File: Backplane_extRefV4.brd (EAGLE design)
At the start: 72.9 x 59.6 mm, 15 parts, among them J1 TFM-125-02-XXX-D-WT

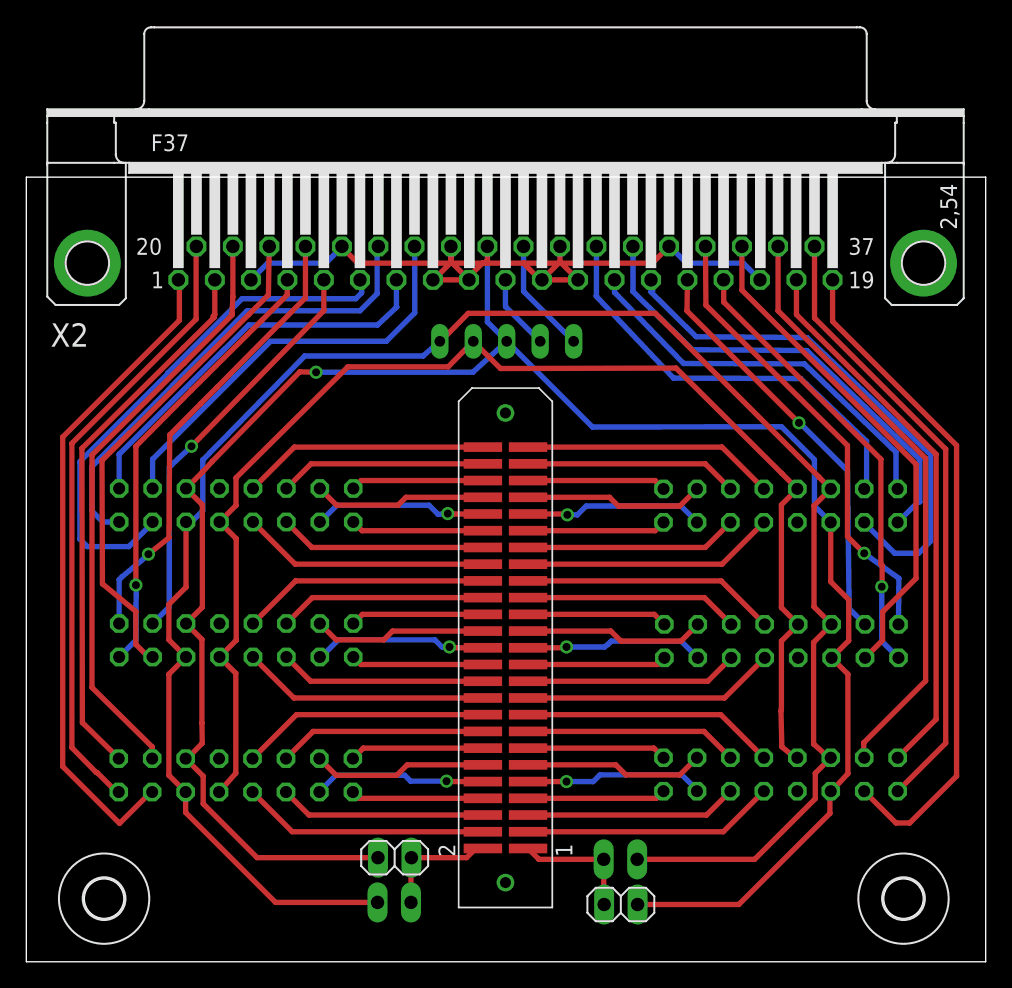
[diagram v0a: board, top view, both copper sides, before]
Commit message: minor labeling and component placement updates. most significant is correcting part position on powerboard so 22uF bypass cap actually connects to ground.
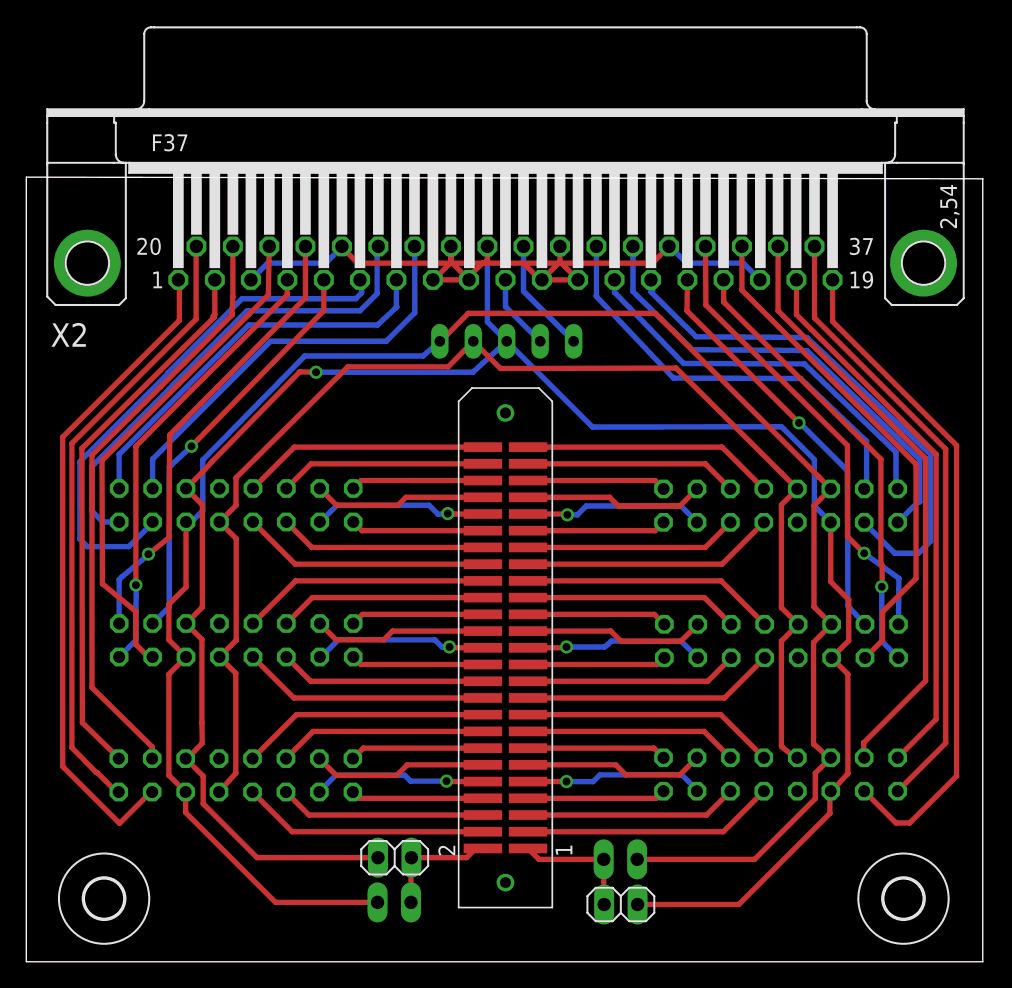
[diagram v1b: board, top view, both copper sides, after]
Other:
- board size 72.9 x 59.6 mm -> 72.6 x 59.6 mm
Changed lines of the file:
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@@
 <board>
 <plain>
-<wire x1="0.0635" y1="0" x2="72.91725" y2="0" width="0" layer="20"/>
-<wire x1="72.91725" y1="0" x2="72.91725" y2="59.58475" width="0" layer="20"/>
-<wire x1="72.91725" y1="59.58475" x2="0.0635" y2="59.58475" width="0" layer="20"/>
+<wire x1="0.0635" y1="0" x2="72.695" y2="0" width="0" layer="20"/>
+<wire x1="72.695" y1="0" x2="72.695" y2="59.45775" width="0" layer="20"/>
+<wire x1="72.695" y1="59.45775" x2="0.0635" y2="59.58475" width="0" layer="20"/>
 <wire x1="0.0635" y1="59.58475" x2="0.0635" y2="0" width="0" layer="20"/>
 <text x="60.706" y="3.39725" size="1.778" layer="26" rot="MR0">G1-&gt;VREF</text>
@@
 </signal>
 <signal name="VCC">
-<wire x1="57.43575" y1="16.3195" x2="57.37225" y2="19.05" width="0.4064" layer="1"/>
-<wire x1="57.37225" y1="19.05" x2="57.404" y2="19.2405" width="0.4064" layer="1"/>
+<wire x1="57.43575" y1="16.3195" x2="57.404" y2="16.383" width="0.4064" layer="1"/>
 <contactref element="SV1" pad="7"/>
 <contactref element="SV2" pad="7"/>
@@
 <wire x1="15.986125" y1="36.750625" x2="15.986125" y2="34.655125" width="0.4064" layer="1"/>
 <wire x1="15.986125" y1="34.655125" x2="14.732" y2="33.401" width="0.4064" layer="1"/>
-<wire x1="57.404" y1="19.2405" x2="57.404" y2="24.35225" width="0.4064" layer="1"/>
+<wire x1="57.404" y1="16.383" x2="57.404" y2="24.35225" width="0.4064" layer="1"/>
 <wire x1="57.404" y1="24.35225" x2="58.674" y2="25.62225" width="0.4064" layer="1"/>
 <wire x1="57.404" y1="26.89225" x2="58.674" y2="25.62225" width="0.4064" layer="1"/>
@@
 <contactref element="SV5" pad="3"/>
 <contactref element="X2" pad="15"/>
-<wire x1="63.754" y1="25.62225" x2="62.5475" y2="26.82875" width="0.4064" layer="16"/>
-<wire x1="62.5475" y1="26.82875" x2="62.4205" y2="37.30625" width="0.4064" layer="16"/>
+<wire x1="63.754" y1="25.62225" x2="62.45225" y2="27.01925" width="0.4064" layer="16"/>
+<wire x1="62.45225" y1="27.01925" x2="62.4205" y2="37.30625" width="0.4064" layer="16"/>
 <wire x1="62.4205" y1="37.30625" x2="58.64225" y2="41.0845" width="0.4064" layer="16"/>
 <wire x1="58.64225" y1="41.0845" x2="58.7375" y2="40.92575" width="0.4064" layer="16"/>
